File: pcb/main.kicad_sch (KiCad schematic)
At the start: 11 parts, among them IC1 DRV5032FB, J3 SJ-3541AS-SMT-TR-67

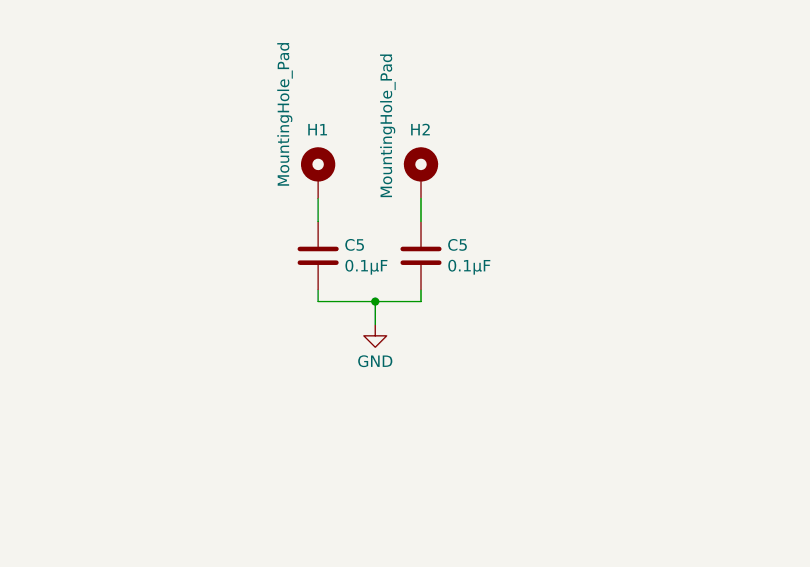
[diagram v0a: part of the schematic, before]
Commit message: Removed capacitor from one of the mountingholes
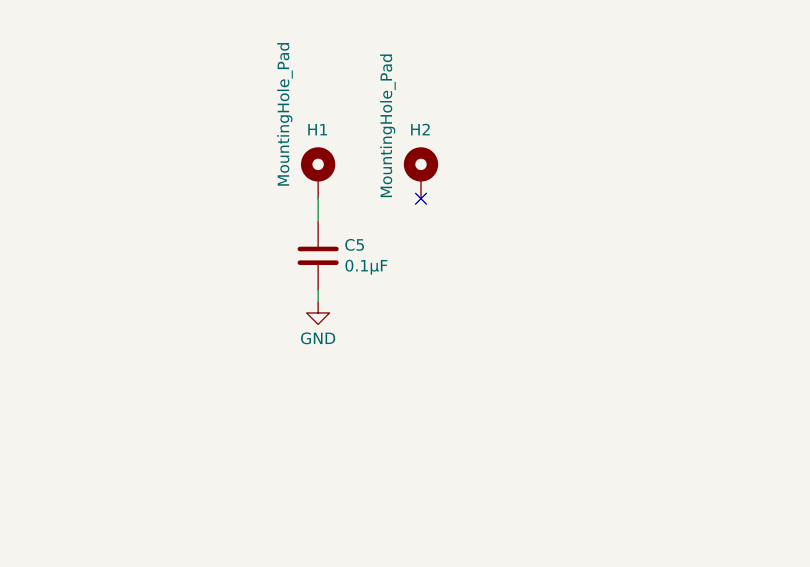
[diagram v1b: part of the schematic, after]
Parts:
- removed C5: 0.1µF, Capacitor_SMD:C_0603_1608Metric, symbol Device:C
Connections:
- no-connect marks 2 -> 3
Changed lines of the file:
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@@
   (junction (at 254 109.22) (diameter 0) (color 0 0 0 0)
   )
-  (junction (at 123.19 142.24) (diameter 0) (color 0 0 0 0)
-  )
   (junction (at 52.07 154.94) (diameter 0) (color 0 0 0 0)
   )
   (junction (at 267.97 147.32) (diameter 0) (color 0 0 0 0)
   )
+  (no_connect (at 128.27 130.81))
   (no_connect (at 251.46 121.92))
   (no_connect (at 251.46 119.38))
@@
     (stroke (width 0) (type default))
   )
-  (wire (pts (xy 128.27 130.81) (xy 128.27 133.35))
-    (stroke (width 0) (type default))
-  )
   (wire (pts (xy 125.73 39.37) (xy 143.51 39.37))
     (stroke (width 0) (type default))
@@
     (stroke (width 0) (type default))
   )
-  (wire (pts (xy 128.27 142.24) (xy 123.19 142.24))
-    (stroke (width 0) (type default))
-  )
   (wire (pts (xy 251.46 111.76) (xy 254 111.76))
     (stroke (width 0) (type default))
@@
     (stroke (width 0) (type default))
   )
-  (wire (pts (xy 123.19 142.24) (xy 123.19 144.78))
-    (stroke (width 0) (type default))
-  )
-  (wire (pts (xy 128.27 140.97) (xy 128.27 142.24))
-    (stroke (width 0) (type default))
-  )
   (wire (pts (xy 49.53 168.91) (xy 58.42 168.91))
     (stroke (width 0) (type default))
@@
   )
   (wire (pts (xy 57.15 38.1) (xy 87.63 38.1))
-    (stroke (width 0) (type default))
-  )
-  (wire (pts (xy 116.84 142.24) (xy 123.19 142.24))
     (stroke (width 0) (type default))
   )
@@
     (effects (font (size 1.27 1.27)) (justify left bottom))
   )
-  (symbol (lib_id "power:GND") (at 123.19 144.78 0) (unit 1)
+  (symbol (lib_id "power:GND") (at 116.84 142.24 0) (unit 1)
     (in_bom yes) (on_board yes) (dnp no) (fields_autoplaced)
-    (property "Reference" "#PWR074" (at 123.19 151.13 0)
+    (property "Reference" "#PWR074" (at 116.84 148.59 0)
       (effects (font (size 1.27 1.27)) hide)
     )
-    (property "Value" "GND" (at 123.19 148.9155 0)
+    (property "Value" "GND" (at 116.84 146.3755 0)
       (effects (font (size 1.27 1.27)))
     )
-    (property "Footprint" "" (at 123.19 144.78 0)
+    (property "Footprint" "" (at 116.84 142.24 0)
       (effects (font (size 1.27 1.27)) hide)
     )
-    (property "Datasheet" "" (at 123.19 144.78 0)
+    (property "Datasheet" "" (at 116.84 142.24 0)
       (effects (font (size 1.27 1.27)) hide)
     )
@@
         )
       )
-    )
-  )
-  (symbol (lib_id "Device:C") (at 128.27 137.16 0) (unit 1)
-    (in_bom yes) (on_board yes) (dnp no)
-    (property "Reference" "C5" (at 131.191 135.9916 0)
-      (effects (font (size 1.27 1.27)) (justify left))
-    )
-    (property "Value" "0.1µF" (at 131.191 138.303 0)
-      (effects (font (size 1.27 1.27)) (justify left))
-    )
-    (property "Footprint" "Capacitor_SMD:C_0603_1608Metric" (at 129.2352 140.97 0)
-      (effects (font (size 1.27 1.27)) hide)
-    )
-    (property "Datasheet" "~" (at 128.27 137.16 0)
-      (effects (font (size 1.27 1.27)) hide)
-    )
-    (pin "1")
-    (pin "2")
-    (instances
-      (project "RP2040_minimal"
-        (path "/966e07a3-e14e-42ec-8301-447655da419c"
-          (reference "C5") (unit 1)
-        )
-      )
-      (project "rep-trap-pcb"
-        (path "/b363dc8f-4a45-4779-a397-ccb82393dab8/eebb1d37-a01d-4adf-be70-a8e8f9293475/e7ccec12-46ad-495a-887c-7169982423a2"
-          (reference "C15") (unit 1)
-        )
-        (path "/b363dc8f-4a45-4779-a397-ccb82393dab8/eebb1d37-a01d-4adf-be70-a8e8f9293475"
-          (reference "C19") (unit 1)
-        )
-      )

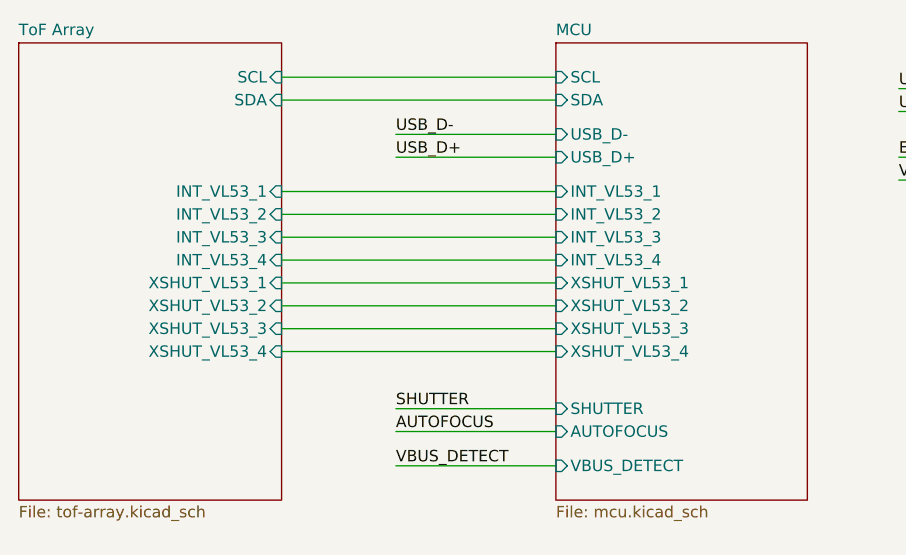
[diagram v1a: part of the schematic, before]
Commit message: Changed net names to match functionallity of active low
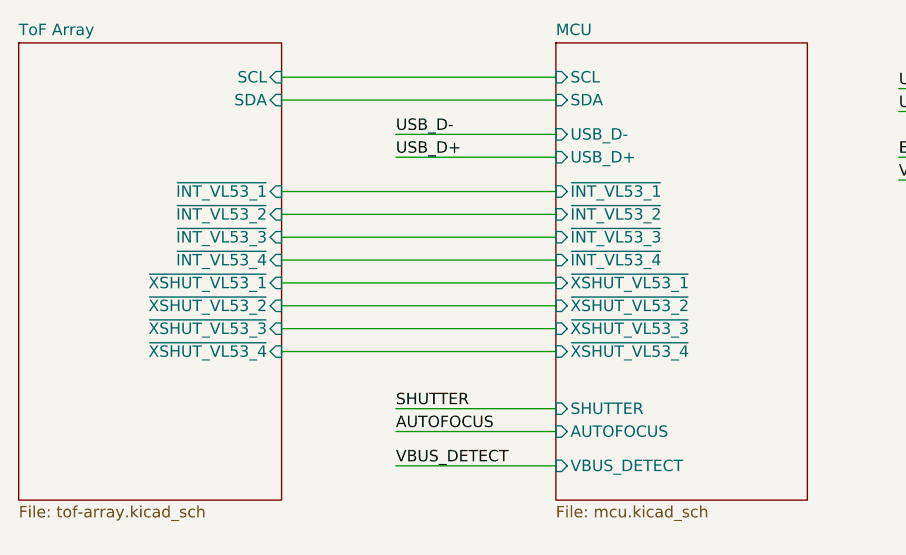
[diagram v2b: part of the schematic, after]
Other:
- sheet MCU ports: added ~{INT_VL53_1}, ~{INT_VL53_2}, ~{INT_VL53_3}, ~{INT_VL53_4}, ~{XSHUT_VL53_1}, ~{XSHUT_VL53_2}, ~{XSHUT_VL53_3}, ~{XSHUT_VL53_4}; removed INT_VL53_1, INT_VL53_2, INT_VL53_3, INT_VL53_4, XSHUT_VL53_1, XSHUT_VL53_2, XSHUT_VL53_3, XSHUT_VL53_4
- sheet ToF Array ports: added ~{INT_VL53_1}, ~{INT_VL53_2}, ~{INT_VL53_3}, ~{INT_VL53_4}, ~{XSHUT_VL53_1}, ~{XSHUT_VL53_2}, ~{XSHUT_VL53_3}, ~{XSHUT_VL53_4}; removed INT_VL53_1, INT_VL53_2, INT_VL53_3, INT_VL53_4, XSHUT_VL53_1, XSHUT_VL53_2, XSHUT_VL53_3, XSHUT_VL53_4
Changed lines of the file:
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@@
       (effects (font (size 1.27 1.27)) (justify right))
     )
-    (pin "INT_VL53_1" input (at 57.15 48.26 0)
+    (pin "~{INT_VL53_1}" input (at 57.15 48.26 0)
       (effects (font (size 1.27 1.27)) (justify right))
     )
-    (pin "INT_VL53_2" input (at 57.15 50.8 0)
+    (pin "~{INT_VL53_2}" input (at 57.15 50.8 0)
       (effects (font (size 1.27 1.27)) (justify right))
     )
-    (pin "INT_VL53_3" input (at 57.15 53.34 0)
+    (pin "~{INT_VL53_3}" input (at 57.15 53.34 0)
       (effects (font (size 1.27 1.27)) (justify right))
     )
-    (pin "INT_VL53_4" input (at 57.15 55.88 0)
+    (pin "~{INT_VL53_4}" input (at 57.15 55.88 0)
       (effects (font (size 1.27 1.27)) (justify right))
     )
-    (pin "XSHUT_VL53_1" input (at 57.15 58.42 0)
+    (pin "~{XSHUT_VL53_1}" input (at 57.15 58.42 0)
       (effects (font (size 1.27 1.27)) (justify right))
     )
-    (pin "XSHUT_VL53_3" input (at 57.15 63.5 0)
+    (pin "~{XSHUT_VL53_3}" input (at 57.15 63.5 0)
       (effects (font (size 1.27 1.27)) (justify right))
     )
-    (pin "XSHUT_VL53_2" input (at 57.15 60.96 0)
+    (pin "~{XSHUT_VL53_2}" input (at 57.15 60.96 0)
       (effects (font (size 1.27 1.27)) (justify right))
     )
-    (pin "XSHUT_VL53_4" input (at 57.15 66.04 0)
+    (pin "~{XSHUT_VL53_4}" input (at 57.15 66.04 0)
       (effects (font (size 1.27 1.27)) (justify right))
     )
@@
       (effects (font (size 1.27 1.27)) (justify left))
     )
-    (pin "INT_VL53_1" input (at 87.63 48.26 180)
+    (pin "~{INT_VL53_1}" input (at 87.63 48.26 180)
       (effects (font (size 1.27 1.27)) (justify left))
     )
-    (pin "INT_VL53_4" input (at 87.63 55.88 180)
+    (pin "~{INT_VL53_4}" input (at 87.63 55.88 180)
       (effects (font (size 1.27 1.27)) (justify left))
     )
-    (pin "XSHUT_VL53_3" input (at 87.63 63.5 180)
+    (pin "~{XSHUT_VL53_3}" input (at 87.63 63.5 180)
       (effects (font (size 1.27 1.27)) (justify left))
     )
-    (pin "XSHUT_VL53_2" input (at 87.63 60.96 180)
+    (pin "~{XSHUT_VL53_2}" input (at 87.63 60.96 180)
       (effects (font (size 1.27 1.27)) (justify left))
     )
-    (pin "INT_VL53_3" input (at 87.63 53.34 180)
+    (pin "~{INT_VL53_3}" input (at 87.63 53.34 180)
       (effects (font (size 1.27 1.27)) (justify left))
     )
-    (pin "XSHUT_VL53_4" input (at 87.63 66.04 180)
+    (pin "~{XSHUT_VL53_4}" input (at 87.63 66.04 180)
       (effects (font (size 1.27 1.27)) (justify left))
     )
-    (pin "XSHUT_VL53_1" input (at 87.63 58.42 180)
+    (pin "~{XSHUT_VL53_1}" input (at 87.63 58.42 180)
       (effects (font (size 1.27 1.27)) (justify left))
     )
-    (pin "INT_VL53_2" input (at 87.63 50.8 180)
+    (pin "~{INT_VL53_2}" input (at 87.63 50.8 180)
       (effects (font (size 1.27 1.27)) (justify left))
     )

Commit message: Updated footprints try to fix DRC
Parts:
- H1, H2: now left out of the parts list
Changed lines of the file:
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@@
   )
   (symbol (lib_id "Mechanical:MountingHole_Pad") (at 128.27 128.27 0) (unit 1)
-    (in_bom yes) (on_board yes) (dnp no)
+    (in_bom no) (on_board yes) (dnp no)
     (property "Reference" "H2" (at 127 123.19 0)
       (effects (font (size 1.27 1.27)) (justify left))
@@
   )
   (symbol (lib_id "Mechanical:MountingHole_Pad") (at 116.84 128.27 0) (unit 1)
-    (in_bom yes) (on_board yes) (dnp no)
+    (in_bom no) (on_board yes) (dnp no)
     (property "Reference" "H1" (at 115.57 123.19 0)
       (effects (font (size 1.27 1.27)) (justify left))

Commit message: Swapped 100-Ohms with 47-Ohms for the optocoupler
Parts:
- IC1: value DRV5032FB -> DRV5032FBLPG
- R23, R24: value 100R -> 47R
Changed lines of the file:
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@@
       (effects (font (size 1.27 1.27)))
     )
-    (property "Value" "100R" (at 204.47 140.97 90)
+    (property "Value" "47R" (at 204.47 140.97 90)
       (effects (font (size 1.27 1.27)))
     )
@@
       (effects (font (size 1.27 1.27)))
     )
-    (property "Value" "DRV5032FB" (at 38.1 158.75 0)
+    (property "Value" "DRV5032FBLPG" (at 38.1 158.75 0)
       (effects (font (size 1.27 1.27)))
     )
@@
       (effects (font (size 1.27 1.27)))
     )
-    (property "Value" "100R" (at 204.47 132.08 90)
+    (property "Value" "47R" (at 204.47 132.08 90)
       (effects (font (size 1.27 1.27)))
     )

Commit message: Added Testpoints on bottom side
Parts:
- added TP1: TP_SHUTTER, TestPoint:TestPoint_Pad_D1.0mm, symbol Connector:TestPoint
- added TP1 (x2): TP_3V3, TestPoint:TestPoint_Pad_D1.0mm, symbol Connector:TestPoint
- added TP1: TP_FOCUS, TestPoint:TestPoint_Pad_D1.0mm, symbol Connector:TestPoint
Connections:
- net AUTOFOCUS: now also TP1.1
- net GND: now also TP1.1
- net SHUTTER: now also TP1.1
- new net +3.3V: TP1.1
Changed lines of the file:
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@@
   (junction (at 60.96 166.37) (diameter 0) (color 0 0 0 0)
+  )
+  (junction (at 185.42 143.51) (diameter 0) (color 0 0 0 0)
+  )
+  (junction (at 185.42 134.62) (diameter 0) (color 0 0 0 0)
   )
   (junction (at 254 109.22) (diameter 0) (color 0 0 0 0)
@@
     (stroke (width 0) (type default))
   )
-  (wire (pts (xy 177.8 143.51) (xy 201.93 143.51))
+  (wire (pts (xy 166.37 143.51) (xy 185.42 143.51))
     (stroke (width 0) (type default))
   )
@@
     (stroke (width 0) (type default))
   )
+  (wire (pts (xy 185.42 140.97) (xy 185.42 143.51))
+    (stroke (width 0) (type default))
+  )
   (wire (pts (xy 49.53 163.83) (xy 52.07 163.83))
     (stroke (width 0) (type default))
@@
     (stroke (width 0) (type default))
   )
+  (wire (pts (xy 85.09 121.92) (xy 85.09 124.46))
+    (stroke (width 0) (type default))
+  )
+  (wire (pts (xy 59.69 119.38) (xy 59.69 123.19))
+    (stroke (width 0) (type default))
+  )
   (wire (pts (xy 267.97 138.43) (xy 267.97 147.32))
     (stroke (width 0) (type default))
@@
     (stroke (width 0) (type default))
   )
+  (wire (pts (xy 185.42 129.54) (xy 185.42 134.62))
+    (stroke (width 0) (type default))
+  )
   (wire (pts (xy 125.73 46.99) (xy 143.51 46.99))
     (stroke (width 0) (type default))
@@
     (stroke (width 0) (type default))
   )
+  (wire (pts (xy 185.42 143.51) (xy 201.93 143.51))
+    (stroke (width 0) (type default))
+  )
   (wire (pts (xy 57.15 60.96) (xy 87.63 60.96))
     (stroke (width 0) (type default))
@@
     (stroke (width 0) (type default))
   )
+  (wire (pts (xy 77.47 124.46) (xy 85.09 124.46))
+    (stroke (width 0) (type default))
+  )
+  (wire (pts (xy 77.47 120.65) (xy 77.47 124.46))
+    (stroke (width 0) (type default))
+  )
   (wire (pts (xy 52.07 152.4) (xy 52.07 154.94))
     (stroke (width 0) (type default))
@@
     (stroke (width 0) (type default))
   )
-  (wire (pts (xy 177.8 134.62) (xy 201.93 134.62))
+  (wire (pts (xy 166.37 134.62) (xy 185.42 134.62))
     (stroke (width 0) (type default))
   )
@@
   )
   (wire (pts (xy 69.85 44.45) (xy 87.63 44.45))
+    (stroke (width 0) (type default))
+  )
+  (wire (pts (xy 185.42 134.62) (xy 201.93 134.62))
     (stroke (width 0) (type default))
   )
@@
     (effects (font (size 1.27 1.27)) (justify left bottom))
   )
-  (label "AUTOFOCUS" (at 177.8 143.51 0) (fields_autoplaced)
+  (label "AUTOFOCUS" (at 166.37 143.51 0) (fields_autoplaced)
     (effects (font (size 1.27 1.27)) (justify left bottom))
   )
@@
     (effects (font (size 1.27 1.27)) (justify right bottom))
   )
-  (label "SHUTTER" (at 177.8 134.62 0) (fields_autoplaced)
+  (label "SHUTTER" (at 166.37 134.62 0) (fields_autoplaced)
     (effects (font (size 1.27 1.27)) (justify left bottom))
   )
@@
   (label "AUTOFOCUS" (at 69.85 74.93 0) (fields_autoplaced)
     (effects (font (size 1.27 1.27)) (justify left bottom))
+  )
+  (symbol (lib_id "Connector:TestPoint") (at 185.42 129.54 0) (unit 1)
+    (in_bom no) (on_board yes) (dnp no) (fields_autoplaced)
+    (property "Reference" "TP1" (at 187.96 124.968 0)
+      (effects (font (size 1.27 1.27)) (justify left))
+    )
+    (property "Value" "TP_SHUTTER" (at 187.96 127.508 0)
+      (effects (font (size 1.27 1.27)) (justify left))
+    )
+    (property "Footprint" "TestPoint:TestPoint_Pad_D1.0mm" (at 190.5 129.54 0)
+      (effects (font (size 1.27 1.27)) hide)
+    )
+    (property "Datasheet" "~" (at 190.5 129.54 0)
+      (effects (font (size 1.27 1.27)) hide)
+    )
+    (pin "1")
+    (instances
+      (project "rep-trap-pcb"
+        (path "/b363dc8f-4a45-4779-a397-ccb82393dab8/eebb1d37-a01d-4adf-be70-a8e8f9293475/e7ccec12-46ad-495a-887c-7169982423a2"
+          (reference "TP1") (unit 1)
+        )
+        (path "/b363dc8f-4a45-4779-a397-ccb82393dab8/eebb1d37-a01d-4adf-be70-a8e8f9293475"
+          (reference "TP15") (unit 1)
+        )
+      )
+    )
   )
   (symbol (lib_id "power:GND") (at 116.84 142.24 0) (unit 1)
@@
         (path "/b363dc8f-4a45-4779-a397-ccb82393dab8/eebb1d37-a01d-4adf-be70-a8e8f9293475"
           (reference "#PWR01") (unit 1)
+        )
+      )
+    )
+  )
+  (symbol (lib_id "Connector:TestPoint") (at 85.09 121.92 0) (unit 1)
+    (in_bom no) (on_board yes) (dnp no) (fields_autoplaced)
+    (property "Reference" "TP1" (at 87.63 117.348 0)
+      (effects (font (size 1.27 1.27)) (justify left))
+    )
+    (property "Value" "TP_3V3" (at 87.63 119.888 0)
+      (effects (font (size 1.27 1.27)) (justify left))
+    )
+    (property "Footprint" "TestPoint:TestPoint_Pad_D1.0mm" (at 90.17 121.92 0)
+      (effects (font (size 1.27 1.27)) hide)
+    )
+    (property "Datasheet" "~" (at 90.17 121.92 0)
+      (effects (font (size 1.27 1.27)) hide)
+    )
+    (pin "1")
+    (instances
+      (project "rep-trap-pcb"
+        (path "/b363dc8f-4a45-4779-a397-ccb82393dab8/eebb1d37-a01d-4adf-be70-a8e8f9293475/e7ccec12-46ad-495a-887c-7169982423a2"
+          (reference "TP1") (unit 1)
+        )
+        (path "/b363dc8f-4a45-4779-a397-ccb82393dab8/eebb1d37-a01d-4adf-be70-a8e8f9293475"
+          (reference "TP3") (unit 1)
+        )
+      )
+    )
+  )
+  (symbol (lib_id "Connector:TestPoint") (at 185.42 140.97 0) (unit 1)
+    (in_bom no) (on_board yes) (dnp no) (fields_autoplaced)
+    (property "Reference" "TP1" (at 187.96 136.398 0)
+      (effects (font (size 1.27 1.27)) (justify left))
+    )
+    (property "Value" "TP_FOCUS" (at 187.96 138.938 0)
+      (effects (font (size 1.27 1.27)) (justify left))
+    )
+    (property "Footprint" "TestPoint:TestPoint_Pad_D1.0mm" (at 190.5 140.97 0)
+      (effects (font (size 1.27 1.27)) hide)
+    )
+    (property "Datasheet" "~" (at 190.5 140.97 0)
+      (effects (font (size 1.27 1.27)) hide)
+    )
+    (pin "1")
+    (instances
+      (project "rep-trap-pcb"
+        (path "/b363dc8f-4a45-4779-a397-ccb82393dab8/eebb1d37-a01d-4adf-be70-a8e8f9293475/e7ccec12-46ad-495a-887c-7169982423a2"
+          (reference "TP1") (unit 1)
+        )
+        (path "/b363dc8f-4a45-4779-a397-ccb82393dab8/eebb1d37-a01d-4adf-be70-a8e8f9293475"
+          (reference "TP16") (unit 1)
+        )
+      )
+    )
+  )
+  (symbol (lib_id "power:+3.3V") (at 77.47 120.65 0) (unit 1)
+    (in_bom yes) (on_board yes) (dnp no) (fields_autoplaced)
+    (property "Reference" "#PWR055" (at 77.47 124.46 0)
+      (effects (font (size 1.27 1.27)) hide)
+    )
+    (property "Value" "+3.3V" (at 77.47 117.1481 0)
+      (effects (font (size 1.27 1.27)))
+    )
+    (property "Footprint" "" (at 77.47 120.65 0)
+      (effects (font (size 1.27 1.27)) hide)
+    )
+    (property "Datasheet" "" (at 77.47 120.65 0)
+      (effects (font (size 1.27 1.27)) hide)
+    )
+    (pin "1")
+    (instances
+      (project "rep-trap-pcb"
+        (path "/b363dc8f-4a45-4779-a397-ccb82393dab8/eebb1d37-a01d-4adf-be70-a8e8f9293475/e7ccec12-46ad-495a-887c-7169982423a2"
+          (reference "#PWR055") (unit 1)
+        )
+        (path "/b363dc8f-4a45-4779-a397-ccb82393dab8/eebb1d37-a01d-4adf-be70-a8e8f9293475"
+          (reference "#PWR017") (unit 1)
         )
       )
@@
     )
   )
+  (symbol (lib_id "power:GND") (at 59.69 123.19 0) (unit 1)
+    (in_bom yes) (on_board yes) (dnp no) (fields_autoplaced)
+    (property "Reference" "#PWR074" (at 59.69 129.54 0)
+      (effects (font (size 1.27 1.27)) hide)
+    )
+    (property "Value" "GND" (at 59.69 127.3255 0)
+      (effects (font (size 1.27 1.27)))
+    )
+    (property "Footprint" "" (at 59.69 123.19 0)
+      (effects (font (size 1.27 1.27)) hide)
+    )
+    (property "Datasheet" "" (at 59.69 123.19 0)
+      (effects (font (size 1.27 1.27)) hide)
+    )
+    (pin "1")
+    (instances
+      (project "rep-trap-pcb"
+        (path "/b363dc8f-4a45-4779-a397-ccb82393dab8"
+          (reference "#PWR074") (unit 1)
+        )
+        (path "/b363dc8f-4a45-4779-a397-ccb82393dab8/eebb1d37-a01d-4adf-be70-a8e8f9293475"
+          (reference "#PWR020") (unit 1)
+        )
+      )
+    )
+  )
   (symbol (lib_id "Device:C") (at 116.84 137.16 0) (unit 1)
     (in_bom yes) (on_board yes) (dnp no)
@@
         )
       )
+    )
+  )
+  (symbol (lib_id "Connector:TestPoint") (at 59.69 119.38 0) (unit 1)
+    (in_bom no) (on_board yes) (dnp no) (fields_autoplaced)
+    (property "Reference" "TP1" (at 62.23 114.808 0)
+      (effects (font (size 1.27 1.27)) (justify left))
+    )
+    (property "Value" "TP_3V3" (at 62.23 117.348 0)
+      (effects (font (size 1.27 1.27)) (justify left))
+    )
+    (property "Footprint" "TestPoint:TestPoint_Pad_D1.0mm" (at 64.77 119.38 0)
+      (effects (font (size 1.27 1.27)) hide)
+    )
+    (property "Datasheet" "~" (at 64.77 119.38 0)
+      (effects (font (size 1.27 1.27)) hide)
+    )
+    (pin "1")
+    (instances
+      (project "rep-trap-pcb"
+        (path "/b363dc8f-4a45-4779-a397-ccb82393dab8/eebb1d37-a01d-4adf-be70-a8e8f9293475/e7ccec12-46ad-495a-887c-7169982423a2"
+          (reference "TP1") (unit 1)
+        )
+        (path "/b363dc8f-4a45-4779-a397-ccb82393dab8/eebb1d37-a01d-4adf-be70-a8e8f9293475"
+          (reference "TP17") (unit 1)
+        )
+      )

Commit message: Update to use KiCad8
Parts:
- renumbered TP1 to TP15, TP1 to TP16, TP1 to TP17, TP1 to TP3
